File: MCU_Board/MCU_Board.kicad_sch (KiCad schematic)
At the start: 0 parts

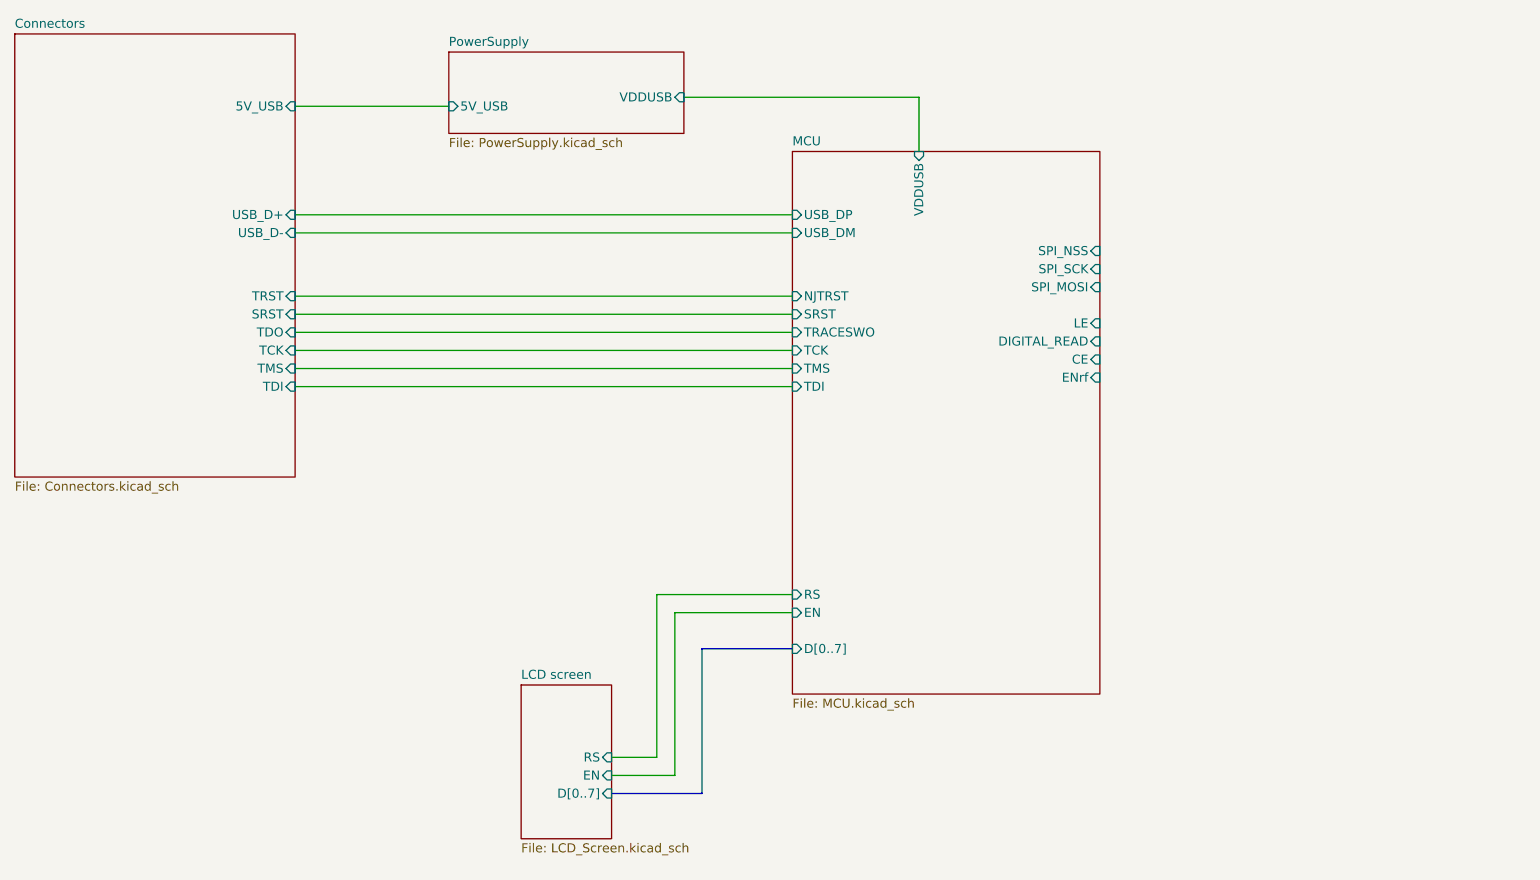
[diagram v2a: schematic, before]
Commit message: Added a header for the VCO controls
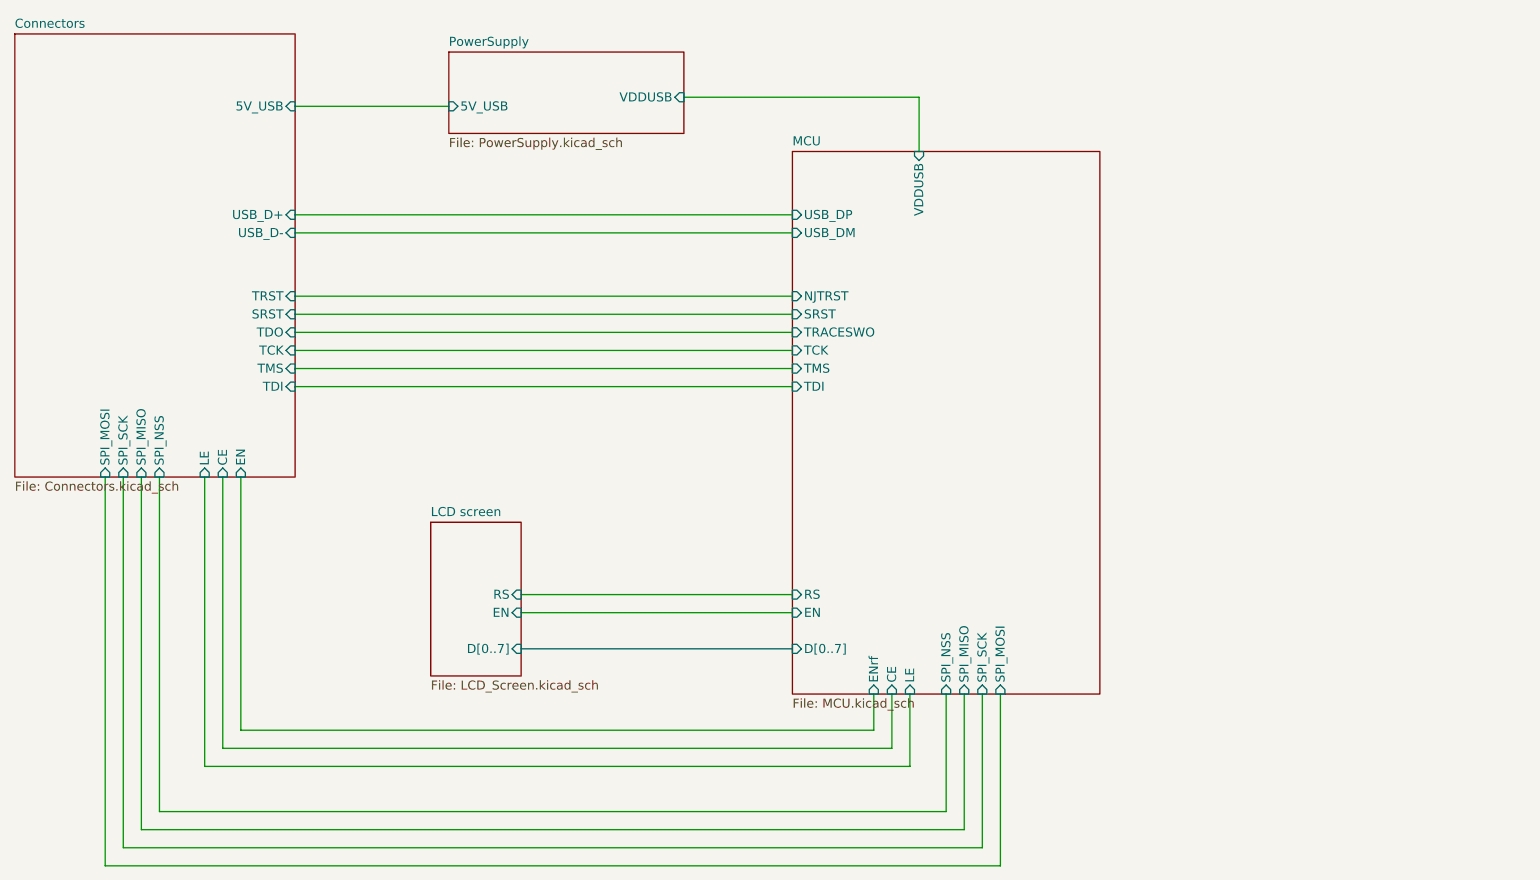
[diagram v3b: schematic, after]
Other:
- sheet Connectors ports: added CE, EN, LE, SPI_MISO, SPI_MOSI, SPI_NSS, SPI_SCK; removed none
- sheet MCU ports: added SPI_MISO; removed DIGITAL_READ
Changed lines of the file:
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@@
     (stroke (width 0) (type default))
   )
-  (wire (pts (xy 104.14 132.08) (xy 113.03 132.08))
-    (stroke (width 0) (type default))
-  )
-  (wire (pts (xy 113.03 109.22) (xy 113.03 132.08))
+  (wire (pts (xy 143.51 128.27) (xy 143.51 120.65))
+    (stroke (width 0) (type default))
+  )
+  (wire (pts (xy 35.56 90.17) (xy 35.56 142.24))
+    (stroke (width 0) (type default))
+  )
+  (wire (pts (xy 153.67 120.65) (xy 153.67 139.7))
+    (stroke (width 0) (type default))
+  )
+  (wire (pts (xy 40.64 137.16) (xy 151.13 137.16))
+    (stroke (width 0) (type default))
+  )
+  (wire (pts (xy 140.97 120.65) (xy 140.97 125.73))
     (stroke (width 0) (type default))
   )
@@
     (stroke (width 0) (type default))
   )
-  (wire (pts (xy 104.14 129.54) (xy 110.49 129.54))
+  (wire (pts (xy 151.13 137.16) (xy 151.13 120.65))
     (stroke (width 0) (type default))
   )
@@
     (stroke (width 0) (type default))
   )
-  (wire (pts (xy 110.49 106.68) (xy 110.49 129.54))
+  (wire (pts (xy 49.53 128.27) (xy 143.51 128.27))
     (stroke (width 0) (type default))
   )
@@
     (stroke (width 0) (type default))
   )
-  (bus (pts (xy 116.84 114.3) (xy 116.84 134.62))
+  (wire (pts (xy 52.07 125.73) (xy 52.07 90.17))
+    (stroke (width 0) (type default))
+  )
+  (wire (pts (xy 35.56 142.24) (xy 156.21 142.24))
+    (stroke (width 0) (type default))
+  )
+  (wire (pts (xy 38.1 139.7) (xy 38.1 90.17))
+    (stroke (width 0) (type default))
+  )
+  (wire (pts (xy 46.99 130.81) (xy 46.99 90.17))
     (stroke (width 0) (type default))
   )
@@
     (stroke (width 0) (type default))
   )
-  (wire (pts (xy 129.54 109.22) (xy 113.03 109.22))
+  (wire (pts (xy 146.05 130.81) (xy 46.99 130.81))
+    (stroke (width 0) (type default))
+  )
+  (wire (pts (xy 140.97 125.73) (xy 52.07 125.73))
+    (stroke (width 0) (type default))
+  )
+  (wire (pts (xy 91.44 109.22) (xy 129.54 109.22))
     (stroke (width 0) (type default))
   )
@@
     (stroke (width 0) (type default))
   )
-  (wire (pts (xy 129.54 106.68) (xy 110.49 106.68))
-    (stroke (width 0) (type default))
-  )
-  (bus (pts (xy 129.54 114.3) (xy 116.84 114.3))
-    (stroke (width 0) (type default))
-  )
-  (bus (pts (xy 104.14 134.62) (xy 116.84 134.62))
+  (wire (pts (xy 156.21 142.24) (xy 156.21 120.65))
+    (stroke (width 0) (type default))
+  )
+  (wire (pts (xy 33.02 144.78) (xy 158.75 144.78))
+    (stroke (width 0) (type default))
+  )
+  (wire (pts (xy 33.02 90.17) (xy 33.02 144.78))
+    (stroke (width 0) (type default))
+  )
+  (wire (pts (xy 153.67 139.7) (xy 38.1 139.7))
+    (stroke (width 0) (type default))
+  )
+  (wire (pts (xy 158.75 120.65) (xy 158.75 144.78))
+    (stroke (width 0) (type default))
+  )
+  (wire (pts (xy 91.44 106.68) (xy 129.54 106.68))
+    (stroke (width 0) (type default))
+  )
+  (bus (pts (xy 91.44 114.3) (xy 129.54 114.3))
+    (stroke (width 0) (type default))
+  )
+  (wire (pts (xy 49.53 90.17) (xy 49.53 128.27))
     (stroke (width 0) (type default))
   )
@@
     (stroke (width 0) (type default))
   )
+  (wire (pts (xy 146.05 120.65) (xy 146.05 130.81))
+    (stroke (width 0) (type default))
+  )
   (wire (pts (xy 147.32 36.83) (xy 147.32 44.45))
+    (stroke (width 0) (type default))
+  )
+  (wire (pts (xy 40.64 90.17) (xy 40.64 137.16))
     (stroke (width 0) (type default))
   )
@@
       (effects (font (size 1.27 1.27)) (justify left))
     )
-    (pin "SPI_NSS" input (at 172.72 58.42 0)
-      (effects (font (size 1.27 1.27)) (justify right))
-    )
-    (pin "SPI_SCK" input (at 172.72 60.96 0)
-      (effects (font (size 1.27 1.27)) (justify right))
-    )
-    (pin "SPI_MOSI" input (at 172.72 63.5 0)
-      (effects (font (size 1.27 1.27)) (justify right))
-    )
     (pin "USB_DM" input (at 129.54 55.88 180)
       (effects (font (size 1.27 1.27)) (justify left))
@@
       (effects (font (size 1.27 1.27)) (justify left))
     )
-    (pin "DIGITAL_READ" input (at 172.72 71.12 0)
-      (effects (font (size 1.27 1.27)) (justify right))
-    )
-    (pin "LE" input (at 172.72 68.58 0)
-      (effects (font (size 1.27 1.27)) (justify right))
-    )
-    (pin "CE" input (at 172.72 73.66 0)
-      (effects (font (size 1.27 1.27)) (justify right))
-    )
-    (pin "ENrf" input (at 172.72 76.2 0)
-      (effects (font (size 1.27 1.27)) (justify right))
-    )
     (pin "NJTRST" input (at 129.54 64.77 180)
       (effects (font (size 1.27 1.27)) (justify left))
@@
     )
     (pin "SRST" input (at 129.54 67.31 180)
+      (effects (font (size 1.27 1.27)) (justify left))
+    )
+    (pin "ENrf" input (at 140.97 120.65 270)
+      (effects (font (size 1.27 1.27)) (justify left))
+    )
+    (pin "CE" input (at 143.51 120.65 270)
+      (effects (font (size 1.27 1.27)) (justify left))
+    )
+    (pin "LE" input (at 146.05 120.65 270)
+      (effects (font (size 1.27 1.27)) (justify left))
+    )
+    (pin "SPI_NSS" input (at 151.13 120.65 270)
+      (effects (font (size 1.27 1.27)) (justify left))
+    )
+    (pin "SPI_SCK" input (at 156.21 120.65 270)
+      (effects (font (size 1.27 1.27)) (justify left))
+    )
+    (pin "SPI_MOSI" input (at 158.75 120.65 270)
+      (effects (font (size 1.27 1.27)) (justify left))
+    )
+    (pin "SPI_MISO" input (at 153.67 120.65 270)
       (effects (font (size 1.27 1.27)) (justify left))
     )
@@
       (effects (font (size 1.27 1.27)) (justify right))
     )
+    (pin "EN" input (at 52.07 90.17 270)
+      (effects (font (size 1.27 1.27)) (justify left))
+    )
+    (pin "CE" input (at 49.53 90.17 270)
+      (effects (font (size 1.27 1.27)) (justify left))
+    )
+    (pin "SPI_SCK" input (at 35.56 90.17 270)
+      (effects (font (size 1.27 1.27)) (justify left))
+    )
+    (pin "LE" input (at 46.99 90.17 270)
+      (effects (font (size 1.27 1.27)) (justify left))
+    )
+    (pin "SPI_MOSI" input (at 33.02 90.17 270)
+      (effects (font (size 1.27 1.27)) (justify left))
+    )
+    (pin "SPI_NSS" input (at 40.64 90.17 270)
+      (effects (font (size 1.27 1.27)) (justify left))
+    )
+    (pin "SPI_MISO" input (at 38.1 90.17 270)
+      (effects (font (size 1.27 1.27)) (justify left))
+    )
     (instances
       (project "MCU_Board"
@@
     )
   )
-  (sheet (at 91.44 119.38) (size 12.7 21.59) (fields_autoplaced)
+  (sheet (at 78.74 96.52) (size 12.7 21.59) (fields_autoplaced)
     (stroke (width 0.1524) (type solid))
     (fill (color 0 0 0 0.0000))
-    (property "Sheetname" "LCD screen" (at 91.44 118.6684 0)
-      (effects (font (size 1.27 1.27)) (justify left bottom))
-    )
-    (property "Sheetfile" "LCD_Screen.kicad_sch" (at 91.44 141.5546 0)
-      (effects (font (size 1.27 1.27)) (justify left top))
-    )
-    (property "Field2" "" (at 91.44 119.38 0)
+    (property "Sheetname" "LCD screen" (at 78.74 95.8084 0)
+      (effects (font (size 1.27 1.27)) (justify left bottom))
+    )
+    (property "Sheetfile" "LCD_Screen.kicad_sch" (at 78.74 118.6946 0)
+      (effects (font (size 1.27 1.27)) (justify left top))
+    )
+    (property "Field2" "" (at 78.74 96.52 0)
       (effects (font (size 1.27 1.27)) hide)
     )
-    (pin "EN" input (at 104.14 132.08 0)
-      (effects (font (size 1.27 1.27)) (justify right))
-    )
-    (pin "RS" input (at 104.14 129.54 0)
-      (effects (font (size 1.27 1.27)) (justify right))
-    )
-    (pin "D[0..7]" input (at 104.14 134.62 0)
-      (effects (font (size 1.27 1.27)) (justify right))
-    )
+    (pin "EN" input (at 91.44 109.22 0)
+      (effects (font (size 1.27 1.27)) (justify right))
+    )
+    (pin "RS" input (at 91.44 106.68 0)
+      (effects (font (size 1.27 1.27)) (justify right))
+    )
+    (pin "D[0..7]" input (at 91.44 114.3 0)
+      (effects (font (size 1.27 1.27)) (justify right))
+    )

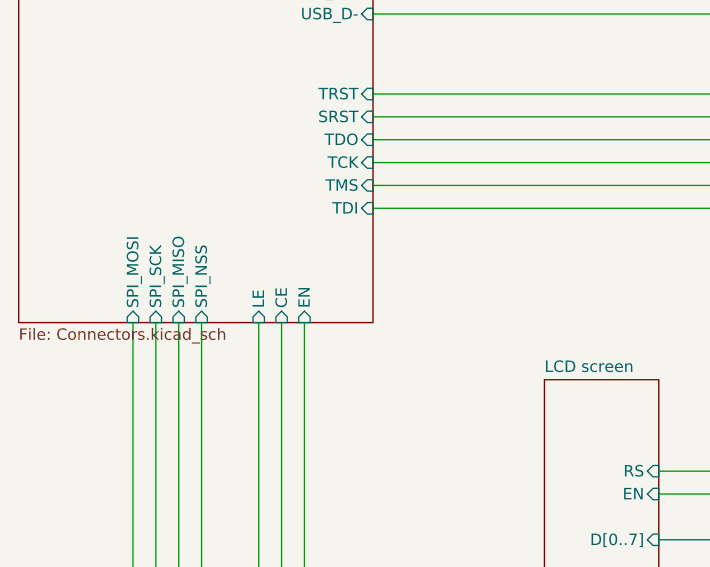
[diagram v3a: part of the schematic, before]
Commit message: Finished MCU board
Finished MCU board and started finishing up the VCO board
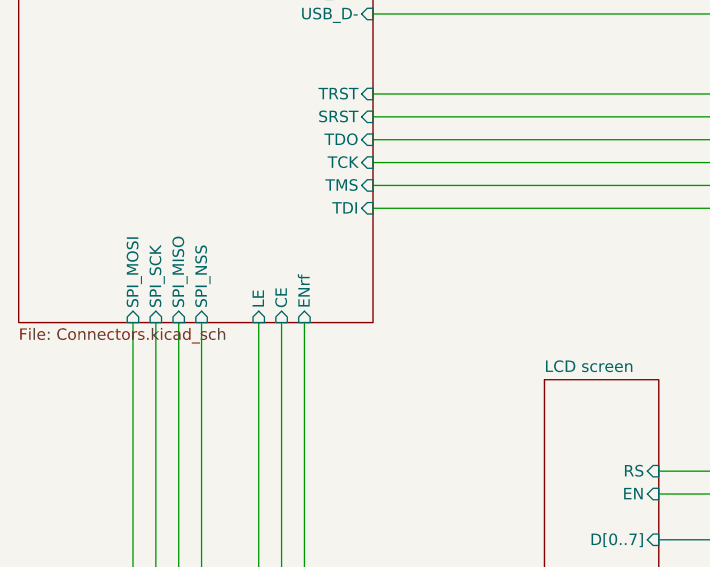
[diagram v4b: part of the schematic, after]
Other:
- sheet Connectors ports: added ENrf; removed EN
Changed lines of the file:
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@@
       (effects (font (size 1.27 1.27)) (justify right))
     )
-    (pin "EN" input (at 52.07 90.17 270)
+    (pin "ENrf" input (at 52.07 90.17 270)
       (effects (font (size 1.27 1.27)) (justify left))
     )
